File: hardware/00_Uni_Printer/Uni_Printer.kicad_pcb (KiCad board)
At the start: 4 copper layers, 96.5 x 78 mm, 133 parts, among them IC1 MAX17503ATP+, IC2 MT25QL256ABA1EW7-0SIT_TR, IC4 TLV1117-33, IC5 LAN8742A, J1 Conn_01x04_Male, J11 LMJ1998824110DL1T39J, J2 FIDUCIAL, J4 Conn_01x06, J5 Conn_02x20_Odd_Even, J6 Conn_02x20_Odd_Even, J6 FIDUCIAL, J7 Conn_02x20_Odd_Even, J8 Conn_02x20_Odd_Even, U1 STM32H743VIT6, U2 74AHC04, U3 74AHC04, U4 TLE9251VSJ, U6 LM2904, U7 LTC2862CS8-1#PBF, Y1 ABM7-25.000MHZ-D2Y-T, Y2 ABM7-25.000MHZ-D2Y-T

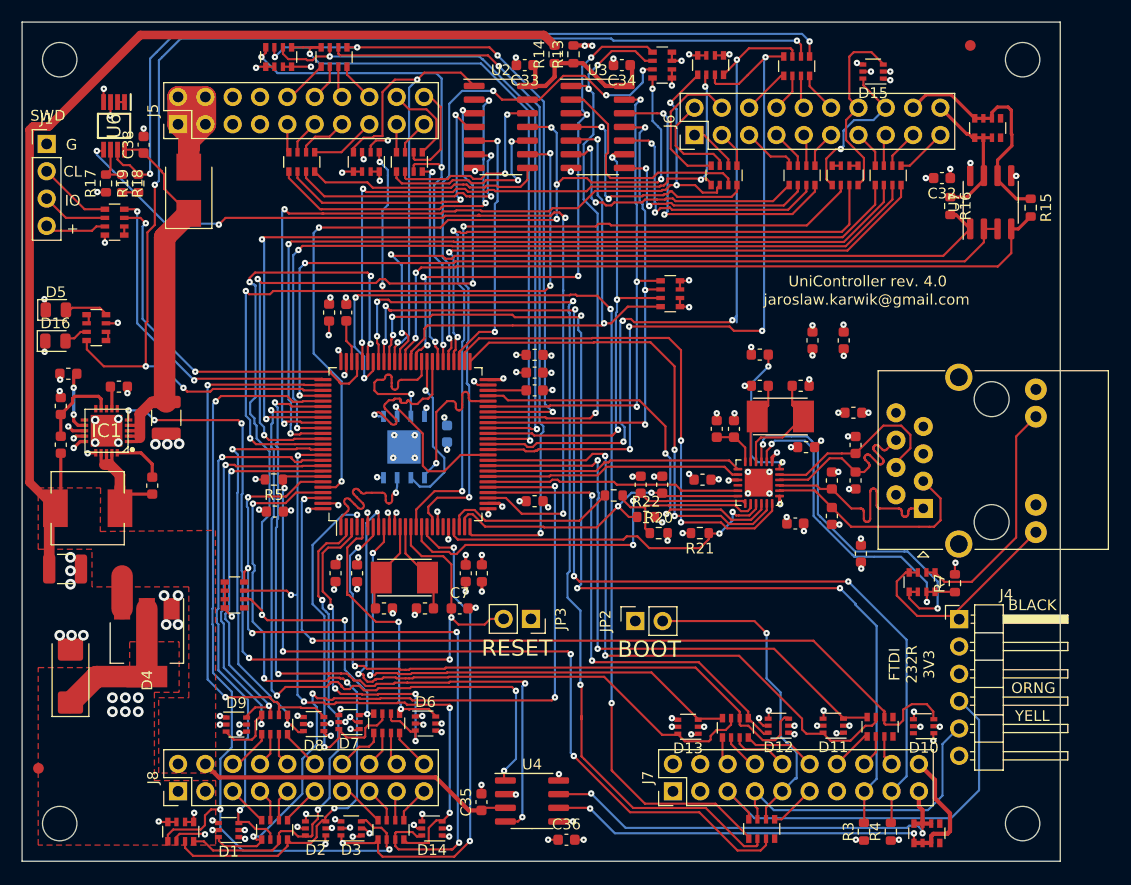
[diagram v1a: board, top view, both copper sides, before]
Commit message: Removed CAN and RS485 drivers
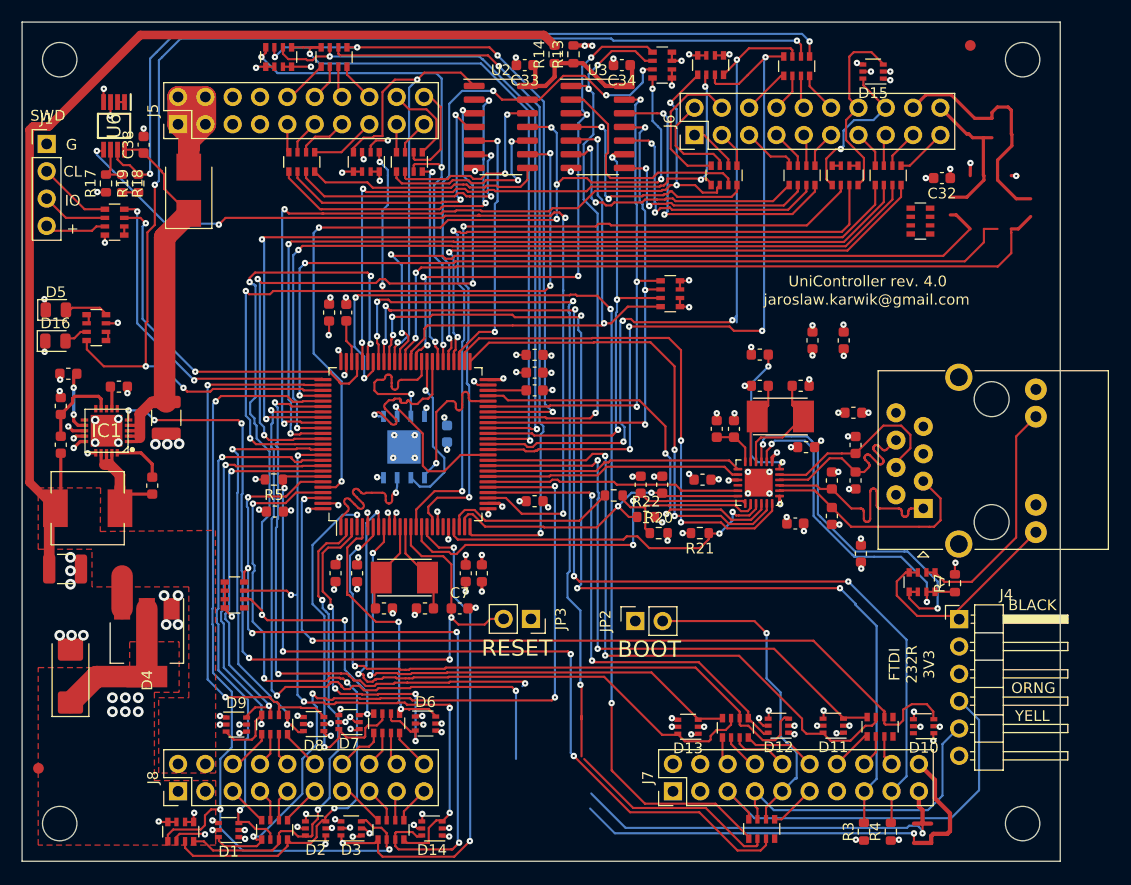
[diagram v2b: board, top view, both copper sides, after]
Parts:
- removed the C35 at (118.2, 141.5)
- removed the C36 at (126.1, 145.0)
- removed the R4 at (169.2, 86.2)
- removed the R4 at (161.8, 86.1)
- removed RN18, RN22: 390R 5%, moje:R_Array_Convex_4x0603
- removed U4: TLE9251VSJ, Package_SO:SOIC-8_3.9x4.9mm_P1.27mm
- removed U7: LTC2862CS8-1#PBF, Package_SO:SOIC-8_3.9x4.9mm_P1.27mm
- added RN6: 100R, moje:R_Array_Convex_4x0603, F.Cu at (159.0, 87.5)
- J5, J6, J7, J8: value Conn_02x20_Odd_Even -> Conn_02x10_Odd_Even
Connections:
- J6 pad 18: /U6_485_A -> Net-(J6-Pad18)
- J6 pad 20: /U6_485_B -> Net-(J6-Pad20)
- J7 pad 19: /CAN_H -> /CAN_RX
- J7 pad 20: /CAN_L -> /CAN_TX
- RN6 pad 2: /LED -> /RS485_DE
- U1 pad 63: /Processor/UART6_TX__PC6 -> /RS485_TX
- U1 pad 64: /Processor/UART6_RX__PC7 -> /RS485_RX
- U1 pad 78: /LED -> /Processor/IO__PC10
- U1 pad 79: Net-(U1-Pad79) -> /RS485_RE
- U1 pad 81: /Processor/FD_CAN_RX_PD0 -> /CAN_RX
- U1 pad 82: /Processor/FD_CAN_TX_PD1 -> /CAN_TX
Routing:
- net /RS485_DE: track 0.00 -> 115.7 mm, vias 0 -> 4
- net /LED: track 115.7 -> 0.00 mm, vias 4 -> 0
- net /CAN_TX: track 0.00 -> 105.7 mm, vias 0 -> 4
- net /CAN_RX: track 0.00 -> 93.2 mm, vias 0 -> 4
- net Net-(U1-Pad79): track 81.1 -> 0.00 mm, vias 2 -> 0
- net /RS485_RE: track 0.00 -> 81.1 mm, vias 0 -> 2
- net /RS485_TX: track 0.00 -> 69.3 mm, vias 0 -> 2
- net /Processor/UART6_TX__PC6: track 69.3 -> 0.00 mm, vias 2 -> 0
- net /Processor/FD_CAN_RX_PD0: track 68.9 -> 0.00 mm, vias 4 -> 0
- net /RS485_RX: track 0.00 -> 68.7 mm, vias 0 -> 2
- net /Processor/UART6_RX__PC7: track 68.7 -> 0.00 mm, vias 2 -> 0
- net /Processor/FD_CAN_TX_PD1: track 64.4 -> 0.00 mm, vias 4 -> 0
- net /CAN_L: track 46.8 -> 0.00 mm, vias 2 -> 0
- net /CAN_H: track 41.3 -> 0.00 mm, vias 2 -> 0
- net +5V: track 133.2 -> 103.3 mm
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
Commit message: Fixes in PCB design
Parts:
- removed C32: 100n / 25V, Capacitor_SMD:C_0603_1608Metric
- moved RN6 4.61 mm to (161.1, 83.4), turned to 90 degrees
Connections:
- RN6 pad 2: /RS485_DE -> /RS485_RE
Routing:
- net /RS485_DE: track 115.7 -> 0.00 mm, vias 4 -> 0
- net /LED: track 0.00 -> 24.9 mm, vias 0 -> 2
- net /CAN_RX: track 93.2 -> 105.6 mm
- net Net-(J6-Pad18): track 22.3 -> 10.7 mm
- net /CAN_TX: track 105.7 -> 114.8 mm
- net Net-(J6-Pad20): track 13.7 -> 6.23 mm
- net /RS485_TX: track 69.3 -> 66.2 mm
- net /IO_CPU7: track 74.1 -> 72.0 mm
- net +3V3: track 69.8 -> 67.8 mm, vias 65 -> 63
- net /RS485_RX: track 68.7 -> 66.9 mm
- net GND: track 89.6 -> 88.1 mm, vias 114 -> 112
- net /RS485_RE: track 81.1 -> 82.2 mm, vias 2 -> 4

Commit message: Prepared for first prototype
Signed-off-by: Jarosław Karwik <jaroslaw.karwik@gmail.com>
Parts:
- moved RN6 6.67 mm to (95.7, 128.9), turned to -90 degrees
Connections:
- U1 pad 78: /Processor/IO__PC10 -> /LED
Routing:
- net /ENC3_CH2.OUT_CPU12_PWM: track 39.7 -> 43.7 mm, vias 2 -> 3
- net /IO_CPU5: track 70.8 -> 73.8 mm, vias 5 -> 4
- net /ENC3_CH1.OUT_CPU11_PWM: track 51.2 -> 53.5 mm
- net +3V3: track 67.8 -> 70.1 mm, vias 63 -> 61
- net /IO_CPU6: track 60.9 -> 62.8 mm, vias 5 -> 4
- net /CAN_TX: track 114.8 -> 114.0 mm
- net /Power_supply/PWR_RESET: track 73.3 -> 72.6 mm
